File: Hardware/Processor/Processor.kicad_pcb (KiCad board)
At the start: 2 copper layers, 85 parts, among them J3 USB_OTG, J5 PIOA, J6 PIOB, J7 PIOC, J8 PIOD, SW1 PB, SW2 PB, SW3 ~RST, U2 ATSAM4E16E

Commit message: Updated BOM & Netlist. Started PCB Layout
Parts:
- added J1: 5V, FritzLib:ConnectorSMD-1x3, F.Cu at (-113.7, -15.3)
- added J2: UART0, FritzLib:ConnectorSMD-1x4, F.Cu at (-98.0, -27.5)
- added J4: JTAGICE3-SWD, FritzLib:ConnectorMicromatch-10, F.Cu at (-87.2, -26.5)
- added JP1: 5V_SEL, FritzLib:ConnectorSMD-1x3, F.Cu at (-105.3, -13.6)
- added L1: 10uH, FritzLib:Inductor_3mmx3mm, F.Cu at (-79.0, -30.2)
- added L2: 2.2uH, Inductors:Inductor_1212, F.Cu at (-80.4, -15.2)
- added Q1: BSSB06NE, TO_SOT_Packages_SMD:SOT-23, F.Cu at (-98.4, -6.02)
- added Q2: BSSB06NE, TO_SOT_Packages_SMD:SOT-23, F.Cu at (-77.4, -22.3)
- added Q3: BSSB06NE, TO_SOT_Packages_SMD:SOT-23, F.Cu at (-72.8, -31.2)
- added Q4: BSSB06NE, TO_SOT_Packages_SMD:SOT-23, F.Cu at (-88.4, -10.5)
- added U1: TXS0102, Housings_SSOP:MSOP-8_3x3mm_Pitch0.65mm, F.Cu at (-69.8, -24.2)
- added U3: 3.0V, TO_SOT_Packages_SMD:SOT-23, F.Cu at (-66.7, -31.2)
- added U4: LM3671, TO_SOT_Packages_SMD:SOT-23-5, F.Cu at (-81.1, -7.81)
- added U5: PRTR5V0U2X, FritzLib:SOT143B, F.Cu at (-98.1, -12.1)
- added Y1: 32.768kHz, FritzLib:FC-135R, F.Cu at (114.0, 107.9)
- added Y2: 12MHz, Crystals:Crystal_HC49-SD_SMD, F.Cu at (122.3, 82.9)
- R14, R17, R19, R21, R22: value R -> 150R
- moved J5 208.9 mm to (-57.6, 139.1)
- moved J6 208.9 mm to (-39.0, 126.3)
- moved J7 208.9 mm to (-33.9, 80.4)
- moved J8 180.9 mm to (200.6, -29.8)
- moved C1 164.4 mm to (-3.81, -29.9)
- moved C23 164.4 mm to (8.66, -41.8)
- moved C3 164.4 mm to (-13.9, -26.4)
- moved C33 164.4 mm to (1.35, -36.0)
- moved C39 164.4 mm to (-3.81, -35.8)
- moved D1 164.4 mm to (-6.10, -12.5)
- moved C12 164.4 mm to (-23.1, -2.41)
- moved C13 164.4 mm to (-25.2, -8.26)
- moved C14 164.4 mm to (-27.6, 3.44)
- moved C15 164.4 mm to (-17.2, -8.26)
- moved C16 164.4 mm to (-10.8, -14.7)
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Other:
- net class Default: clearance 0.2 -> 0.1524; trace_width 0.25 -> 0.1524; via_dia 0.8 -> 0.508; via_drill 0.4 -> 0.3302
- rule pad_to_mask_clearance: 0.2 -> 0.0762
- rule trace_clearance: 0.2 -> 0.1524
- rule trace_min: 0.2 -> 0.1524
- rule via_min_drill: 0.3 -> 0.3302
- rule via_min_size: 0.4 -> 0.508

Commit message: Removed backup files. Updated values of xtal ext caps
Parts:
- C10, C11: value 3.9pF -> 27pF
- C19, C20: value 18pF -> 12pF
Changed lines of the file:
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@@
     (links 348)
     (no_connects 348)
-    (area -119.382577 -58.537401 207.4949 163.937241)
+    (area 0 0 0 0)
     (thickness 1.6)
     (drawings 0)
@@
       (effects (font (size 1 1) (thickness 0.15)))
     )
-    (fp_text value 3.9pF (at 0 1.9 90) (layer F.Fab)
+    (fp_text value 27pF (at 0 1.9 90) (layer F.Fab)
       (effects (font (size 1 1) (thickness 0.15)))
     )
@@
       (effects (font (size 1 1) (thickness 0.15)))
     )
-    (fp_text value 3.9pF (at 0 1.9 270) (layer F.Fab)
+    (fp_text value 27pF (at 0 1.9 270) (layer F.Fab)
       (effects (font (size 1 1) (thickness 0.15)))
     )
@@
       (effects (font (size 1 1) (thickness 0.15)))
     )
-    (fp_text value 18pF (at 0 1.9) (layer F.Fab)
+    (fp_text value 12pF (at 0 1.9) (layer F.Fab)
       (effects (font (size 1 1) (thickness 0.15)))
     )
@@
       (effects (font (size 1 1) (thickness 0.15)))
     )
-    (fp_text value 18pF (at 0 1.9 180) (layer F.Fab)
-      (effects (font (size 1 1) (thickness 0.15)))
-    )
+    (fp_text value 12pF (at 0 1.9 180) (layer F.Fab)
+      (effects (font (size 1 1) (thickness 0.15)))
+    )

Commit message: Completed initial component placement
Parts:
- removed C29: 100nF, Capacitors_SMD:C_0603
- moved J2 309.7 mm to (172.7, 122.8), turned to 270 degrees
- moved J1 286.6 mm to (160.1, 69.2)
- moved J4 286.4 mm to (181.6, 72.4), turned to 90 degrees
- moved U1 269.6 mm to (156.6, 122.2), turned to 180 degrees
- moved SW3 263.2 mm to (171.8, 106.4)
- moved JP1 261.0 mm to (142.2, 69.2), turned to 180 degrees
- moved L2 255.3 mm to (156.5, 80.0)
- moved U4 246.6 mm to (149.9, 78.7)
- moved U5 241.3 mm to (127.8, 72.6), turned to 90 degrees
- moved C9 234.8 mm to (151.1, 122.6), turned to 180 degrees
- moved L1 229.5 mm to (120.9, 82.5)
- moved J3 228.3 mm to (128.4, 65.3), turned to 180 degrees
- moved J5 227.1 mm to (169.5, 137.1), turned to 270 degrees
- moved C37 224.7 mm to (165.7, 108.0), turned to 270 degrees
- moved R5 223.9 mm to (162.1, 120.1), turned to 180 degrees
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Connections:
- U5 pad 4: +5V -> /VBUS
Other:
- board outline added: 128.3 x 80.6 mm
- copper layers 2 -> 4

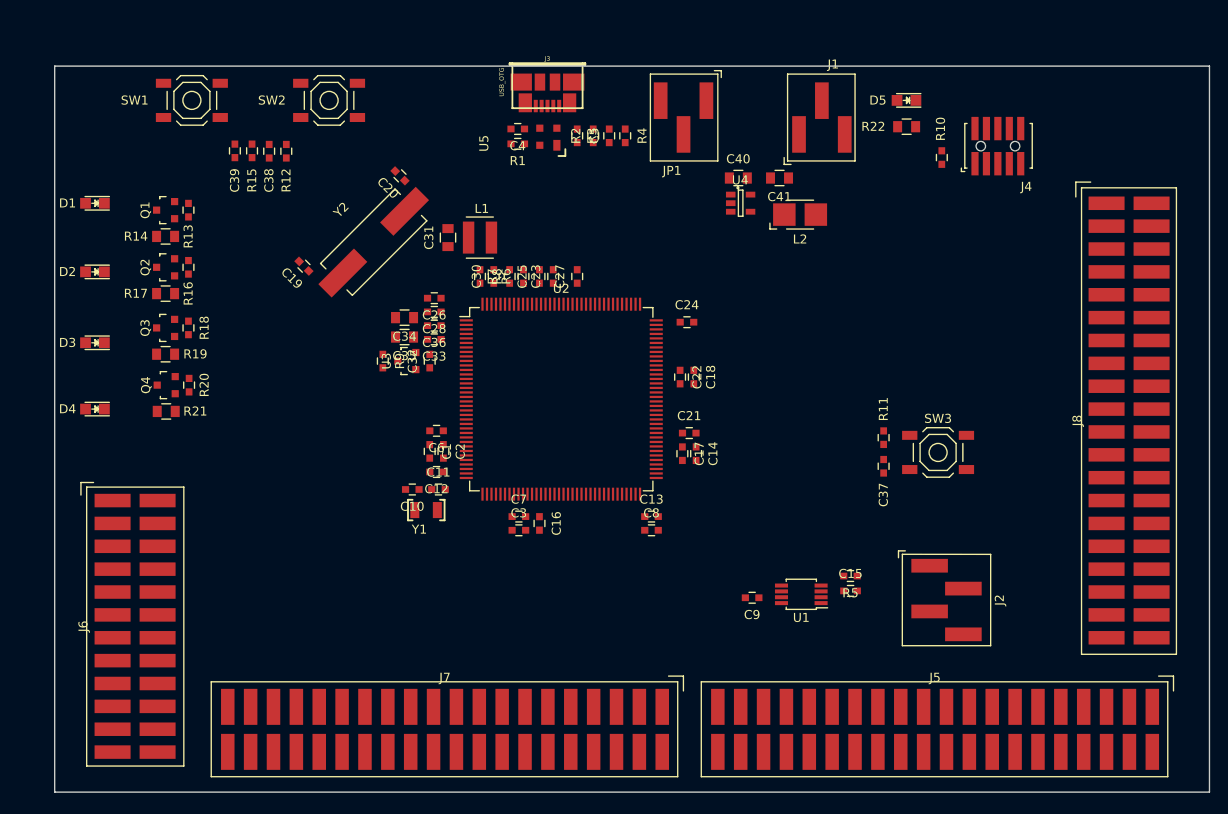
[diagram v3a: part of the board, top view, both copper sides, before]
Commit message: Modified layout to fit 4-layer EasyEDA board
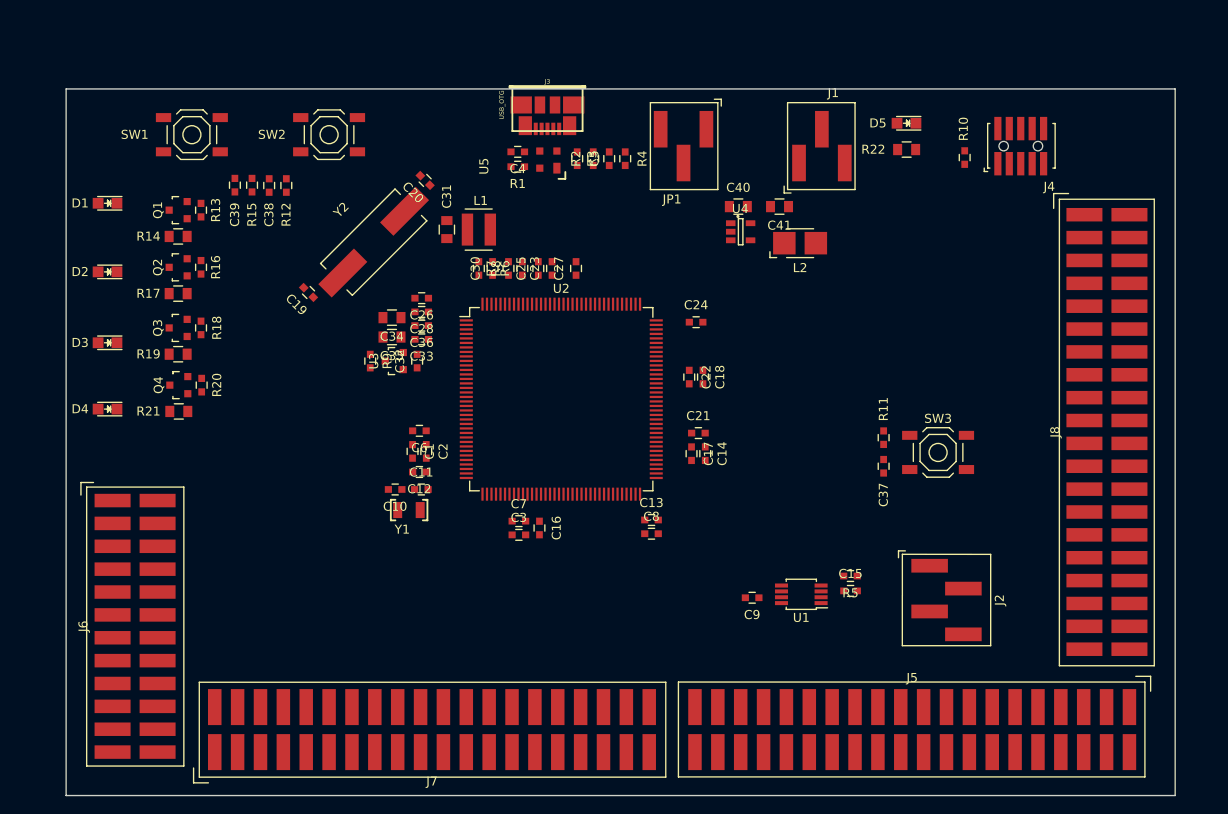
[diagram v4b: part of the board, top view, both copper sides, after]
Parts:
- moved C38 3.81 mm to (97.5, 76.8)
- moved C39 3.81 mm to (93.7, 76.7)
- moved R12 3.81 mm to (99.4, 76.8)
- moved R15 3.81 mm to (95.6, 76.7)
- moved SW1 3.81 mm to (88.9, 71.1)
- moved SW2 3.81 mm to (104.1, 71.1)
- moved C40 3.17 mm to (149.6, 79.1)
- moved C41 3.17 mm to (154.2, 79.1)
- moved J1 3.17 mm to (160.1, 72.4)
- moved JP1 3.17 mm to (142.2, 72.4)
- moved L2 3.17 mm to (156.5, 83.2)
- moved U4 3.17 mm to (149.9, 81.9)
- moved C19 2.96 mm to (101.9, 88.6)
- moved C20 2.84 mm to (114.8, 76.2)
- moved J8 2.77 mm to (190.5, 106.1)
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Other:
- board size 128.3 x 80.6 mm -> 123.2 x 78.5 mm

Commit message: Started routing
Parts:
- moved R4 1.02 mm to (138.0, 73.8)
- moved C5 1.02 mm to (132.7, 73.8)
- moved R2 1.02 mm to (134.5, 73.8)
- moved R3 1.02 mm to (136.3, 73.8)
- moved C19 0.25 mm to (102.1, 88.6)
- moved U5 0.22 mm to (128.1, 75.1)
- moved R13 0.13 mm to (90.0, 79.5)
- moved R16 0.13 mm to (90.0, 85.9)
- moved R18 0.13 mm to (90.0, 92.6)
- moved C2 0.13 mm to (115.1, 106.3)
- moved R20 0.06 mm to (90.0, 98.9)
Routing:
- net /USBD-: track 0.00 -> 17.3 mm
- net /USBD+: track 0.00 -> 17.3 mm
- net /DD-: track 0.00 -> 3.51 mm
- net /DD+: track 0.00 -> 3.47 mm
- net GND: track 0.00 -> 0.72 mm
- added copper zone on B.Cu, net GND
- added copper zone on F.Cu, net GND
- added copper zone on In1.Cu, net GND
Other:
- board text added: "0.01 0.035 0.18 0.017 1.12 0.017 0.18 0.035 0.01"
- board text added: "EasyEDA 1.6mm 1oz 4 Layer Stackup: ------------------------ Layer Thickness (mm) ------------------------ Top Soldermask Top Layer Prepreg Inner1 Core Inner2 Prepreg Bottom Layer Bottom Soldermask"
- board text added: "USB: 90 Ohm diff impedance nominal. w/stackup, trace width: 8 mil, & diff space: 7.5 mil Calculated 89.739 Zdiff, 54.313 Zo --- Keepout should extend minimum 30 mil around usb traces"
